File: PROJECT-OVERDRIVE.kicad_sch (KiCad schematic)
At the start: 87 parts, among them J1 PJ-327A0-SMT, J2 USB_C_Receptacle_USB2.0_16P, J3 Conn_02x10_Odd_Even, K1 G6S-2, P1 SSD1306_ribbon, Q1 AO3401A, Q2 AO3401A, Q3 S8050, U1 CH32V30xVxTx, U2 PCM5102APWR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

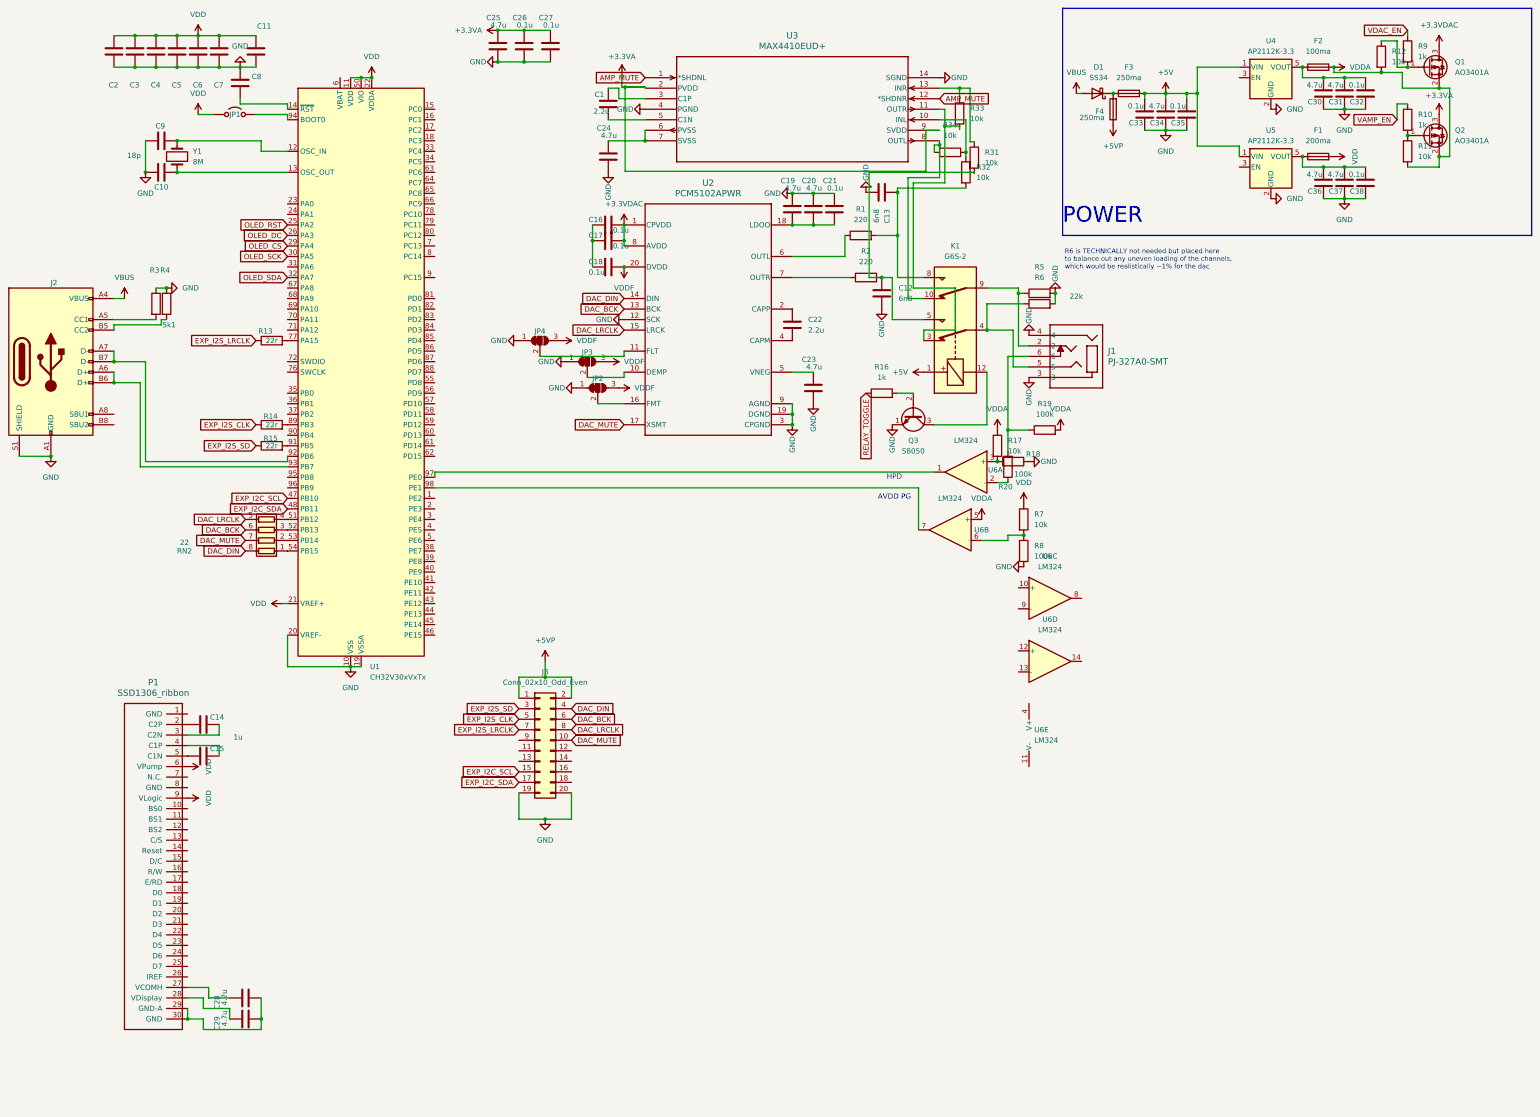
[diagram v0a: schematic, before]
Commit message: wired up the led bus on the mcu side, started spi(flash and oled) wiring
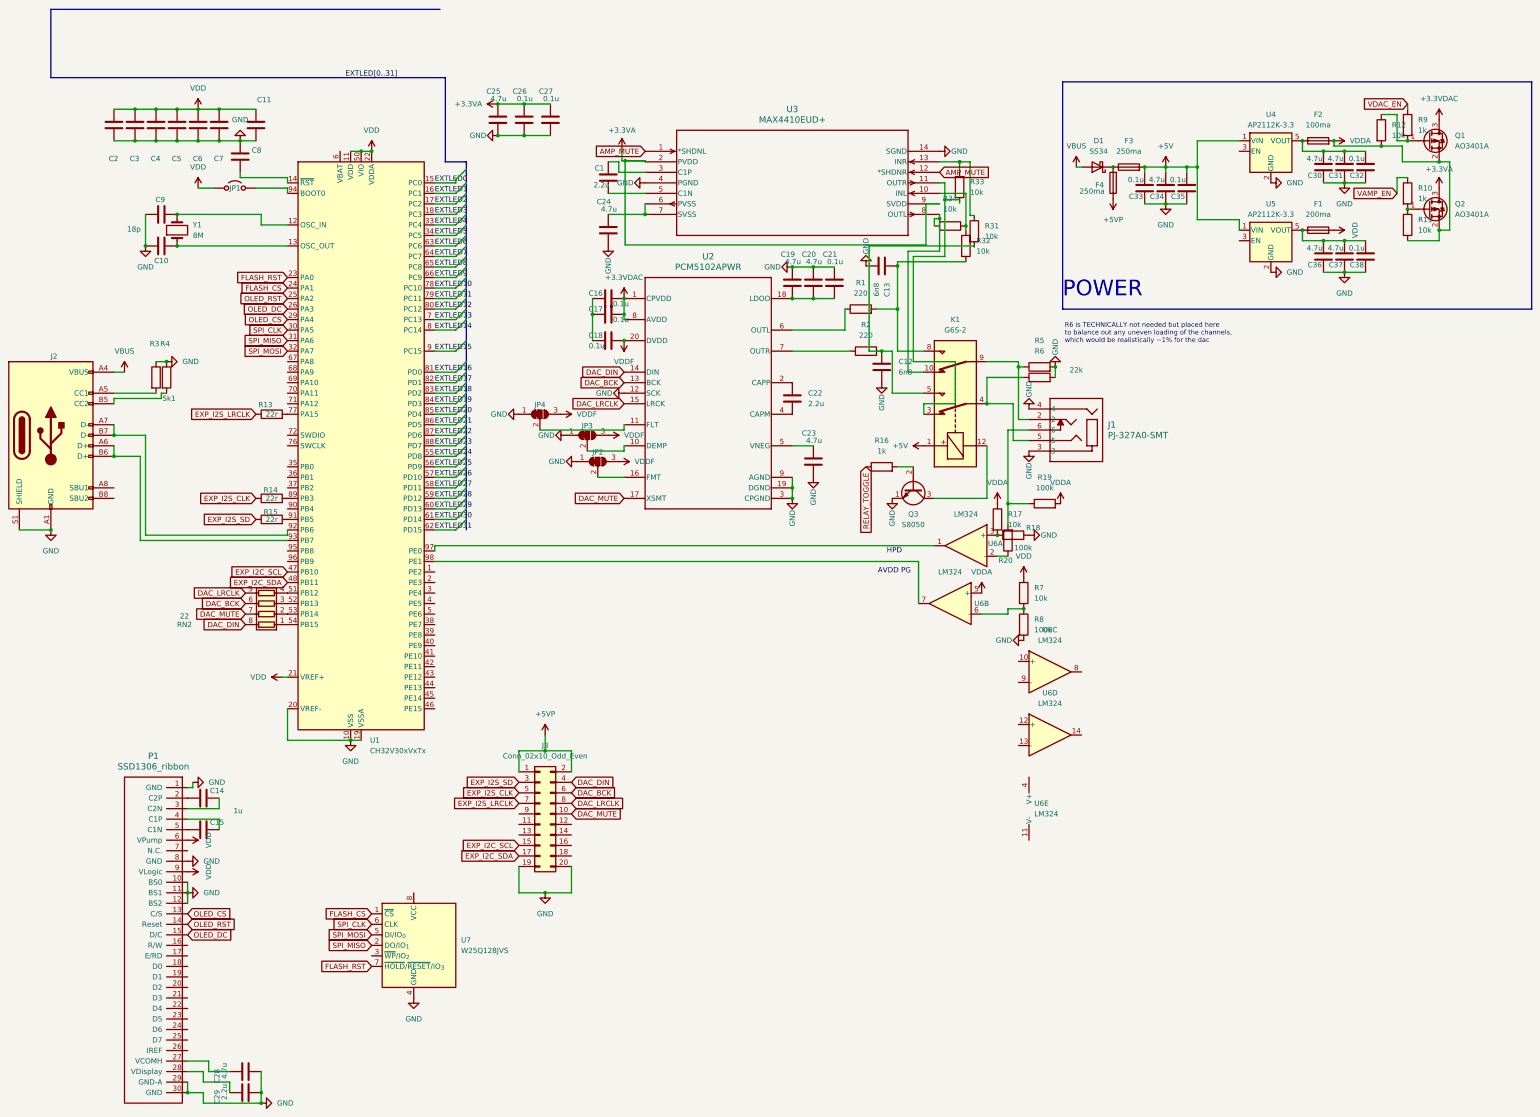
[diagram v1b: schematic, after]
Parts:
- added U7: W25Q128JVS, Package_SO:SOIC-8_5.3x5.3mm_P1.27mm, symbol Memory_Flash:W25Q128JVS
- C29: value 4.7u -> 2.2u
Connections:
- net GND: now also C28.2, C29.2, P1.1 (GND), P1.10 (BS0), P1.11 (BS1), P1.12 (BS2), P1.29 (GND-A), P1.30 (GND), P1.8 (GND), U7.4 (GND)
- net OLED_CS: now also P1.13 (C/S)
- net OLED_DC: now also P1.15 (D/C)
- net OLED_RST: now also P1.14 (Reset)
- net EXTLED0: now reaches U1.15 (PC0)
- net EXTLED1: now reaches U1.16 (PC1)
- net EXTLED2: now reaches U1.17 (PC2)
- net EXTLED3: now reaches U1.18 (PC3)
- net FLASH_RST: now reaches U1.23 (PA0)
- net FLASH_RST: now also U7.7 (~{HOLD}/~{RESET}/IO_{3})
- net FLASH_CS: now reaches U1.24 (PA1)
- net FLASH_CS: now also U7.1 (~{CS})
- net SPI_MISO: now reaches U1.31 (PA6)
- net SPI_MISO: now also U7.2 (DO/IO_{1})
- net EXTLED4: now reaches U1.33 (PC4)
- net EXTLED5: now reaches U1.34 (PC5)
- net EXTLED24: now reaches U1.55 (PD8)
- net EXTLED25: now reaches U1.56 (PD9)
- net EXTLED26: now reaches U1.57 (PD10)
- net EXTLED27: now reaches U1.58 (PD11)
- net EXTLED28: now reaches U1.59 (PD12)
- net EXTLED29: now reaches U1.60 (PD13)
- net EXTLED30: now reaches U1.61 (PD14)
- net EXTLED31: now reaches U1.62 (PD15)
- net EXTLED6: now reaches U1.63 (PC6)
- net EXTLED7: now reaches U1.64 (PC7)
- net EXTLED8: now reaches U1.65 (PC8)
- net EXTLED9: now reaches U1.66 (PC9)
- net EXTLED13: now reaches U1.7 (PC13)
- net EXTLED10: now reaches U1.78 (PC10)
- net EXTLED11: now reaches U1.79 (PC11)
- net EXTLED14: now reaches U1.8 (PC14)
- net EXTLED12: now reaches U1.80 (PC12)
- net EXTLED16: now reaches U1.81 (PD0)
- net EXTLED17: now reaches U1.82 (PD1)
- net EXTLED18: now reaches U1.83 (PD2)
- net EXTLED19: now reaches U1.84 (PD3)
- net EXTLED20: now reaches U1.85 (PD4)
- net EXTLED21: now reaches U1.86 (PD5)
- net EXTLED22: now reaches U1.87 (PD6)
- net EXTLED23: now reaches U1.88 (PD7)
- net EXTLED15: now reaches U1.9 (PC15)
- net OLED_SCK renamed SPI_CLK
- net SPI_CLK: now also U7.6 (CLK)
- net OLED_SDA renamed SPI_MOSI
- net SPI_MOSI: now also U7.5 (DI/IO_{0})
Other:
- moved on the sheet: C1, C10, C11, C12, C13, C14, C15, C16, C17, C18, C19, C2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

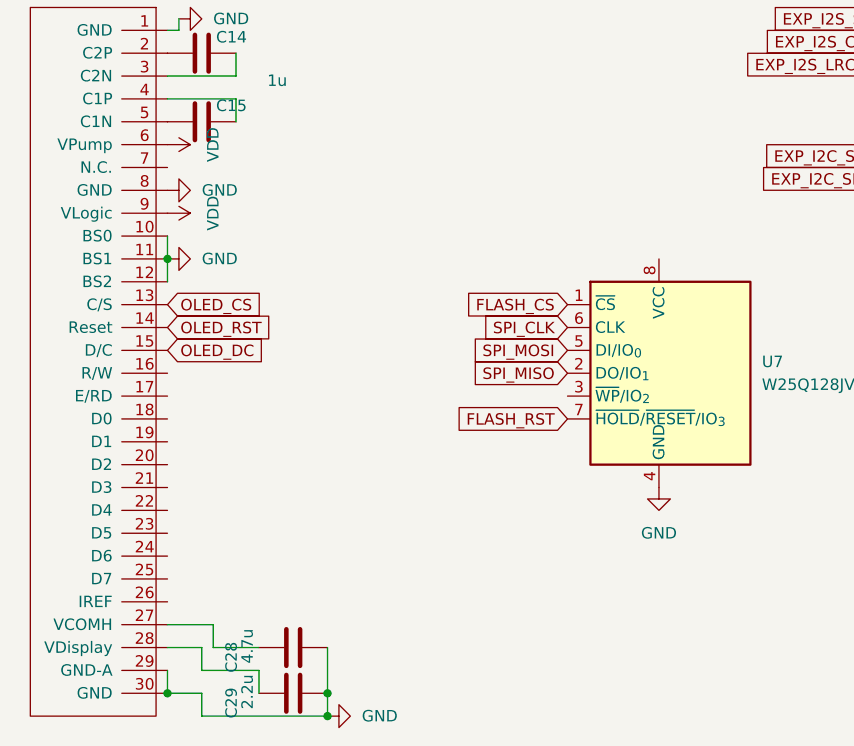
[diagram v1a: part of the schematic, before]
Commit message: spi connections finished
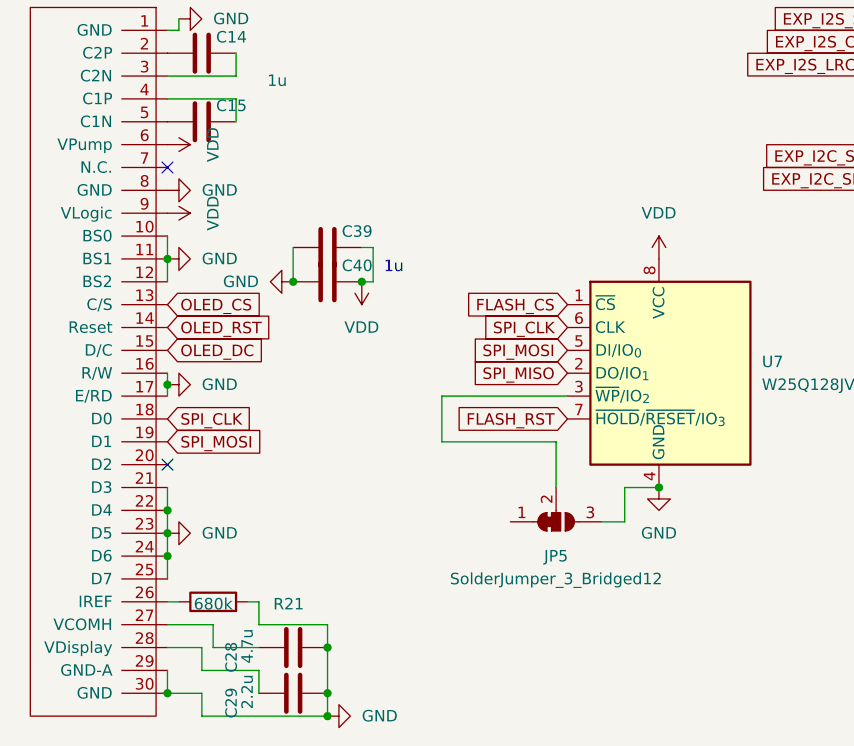
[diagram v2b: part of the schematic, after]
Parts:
- added C39, C40: 1u, Capacitor_SMD:C_0603_1608Metric, symbol Device:C
- added JP5: SolderJumper_3_Bridged12, Jumper:SolderJumper-3_P1.3mm_Bridged12_RoundedPad1.0x1.5mm, symbol Jumper:SolderJumper_3_Bridged12
- added R21: 680k, Resistor_SMD:R_0805_2012Metric, symbol Device:R
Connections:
- net GND: now also P1.16 (R/W), P1.17 (E/RD), P1.21 (D3), P1.22 (D4), P1.23 (D5), P1.24 (D6), P1.25 (D7), C39.1, C40.1, JP5.3 (B), R21.2
- net SPI_CLK: now also P1.18 (D0)
- net SPI_MOSI: now also P1.19 (D1)
- net VDD: now also U7.8 (VCC), C39.2, C40.2
- net at P1.26 (IREF): now also R21.1
- net at U7.3 (~{WP}/IO_{2}): now also JP5.2 (C)
- no-connect marks 0 -> 2
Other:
- note added: "1u"
